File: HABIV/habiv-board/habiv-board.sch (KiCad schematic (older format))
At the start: 129 parts, among them IC1 RTC_PCF8523T, J1 Micro_SD_Card_Det, J10 Conn_01x02_Female, J11 Conn_01x02_Female, J12 Conn_01x02_Female, J13 Conn_01x02_Female, J14 Conn_01x02_Female, J15 Conn_01x02_Female, J16 Conn_01x02_Female, J17 Conn_01x03_Male, J18 Conn_01x03_Male, J19 Conn_01x03_Male, J2 Conn_ARM_JTAG_SWD_20, J20 Conn_01x05_Male, J21 Conn_01x04_Male, J3 Conn_01x02_Male, J4 Conn_01x16_Male, J5 Conn_01x03_Male, J6 Conn_01x16_Male, J7 Conn_01x16_Male, J8 Conn_01x02_Female, J9 Conn_01x02_Male, Q1 32.768KHz, SW1 SW_DPST_x2, U1 STM32F401RET6, U2 MAX31855, U3 FGPMMOPA6H, U4 TPS564208, U5 TPS564208, U6 LSM9DS1TR, U7 MS560702BA03-00, Y1 32.768MHz

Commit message: Turned IMU into breakout pins, minor changes, unfinished!
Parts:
- removed C11, C12, C19: 100n, Capacitor_SMD:C_0805_2012Metric, symbol Device:C_Small
- removed C15: 10u, Capacitor_SMD:C_0805_2012Metric, symbol Device:C_Small
- removed C18: 10n, Capacitor_SMD:C_0805_2012Metric, symbol Device:C_Small
- removed R25, R32, R33, R37: 0, Resistor_SMD:R_0805_2012Metric, symbol Device:R
- removed U6: LSM9DS1TR, digikey-footprints:LGA-24_3x3.5mm_LSM9DS1, symbol dk_Motion-Sensors-IMUs-Inertial-Measurement-Units:LSM9DS1TR
- added J22: Conn_01x09_Male, Connector_PinHeader_2.54mm:PinHeader_1x09_P2.54mm_Vertical, symbol Connector:Conn_01x09_Male
- added JP1: Jumper, Connector_PinHeader_2.54mm:PinHeader_1x02_P2.54mm_Vertical, symbol Device:Jumper
- added R102, R103: 10K, Resistor_SMD:R_0805_2012Metric_Pad1.15x1.40mm_HandSolder, symbol Device:R
- LED1: footprint Adafruit Ultimate GPS:CHIPLED_0805 -> LED_SMD:LED_0805_2012Metric_Pad1.15x1.40mm_HandSolder
- R104: renamed from 10k4; value R8 -> 10K; footprint Resistor_SMD:R_0805_2012Metric -> Resistor_SMD:R_0805_2012Metric_Pad1.15x1.40mm_HandSolder
- R4: renamed from R?; footprint (none) -> Resistor_SMD:R_0805_2012Metric_Pad1.15x1.40mm_HandSolder
- R5: renamed from R?; footprint (none) -> Resistor_SMD:R_0805_2012Metric
- R6: renamed from 10k2; value R6 -> 10K
- R7: renamed from 10k3; value R7 -> 10K
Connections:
- net +3V3: now also C7.1, J22.1 (Pin_1), J22.6 (Pin_6), J22.7 (Pin_7), JP1.1; no longer 10nF1.2, 1uF1.2, 22uH1.1, U1.13 (VDDA/VREF+)
- net GND: now also J22.3 (Pin_3)
- net PB8: now also J22.4 (Pin_4)
- net PB9: now also J22.5 (Pin_5)
- net PC2: now also J22.8 (Pin_8)
- net PC3: now also J22.9 (Pin_9)
- net at U3.P$1 (VCC): now also JP1.2; no longer C7.1
- net at C8.1, C9.1, J9.2 (Pin_2)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: now also R102.2, R103.2; no longer U4.5 (EN), U5.5 (EN)
- new net: 10nF1.2, 1uF1.2, 22uH1.1, U1.13 (VDDA/VREF+)
- new net: R102.1, U4.5 (EN)
- new net: R103.1, U5.5 (EN)
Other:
- note added: "IMU"
- note removed: "C18: 1nF Minimum must be guaranteed under an 11V bias condition\n"
- moved on the sheet: C8, C9, J9

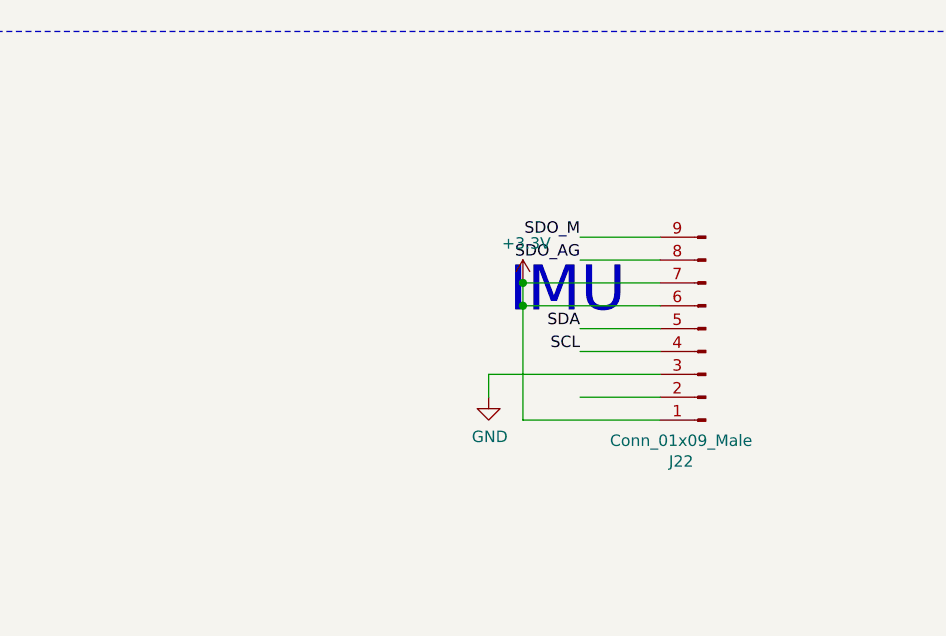
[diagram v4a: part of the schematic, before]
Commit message: Changed IMU pinout, fixed some grounding issues
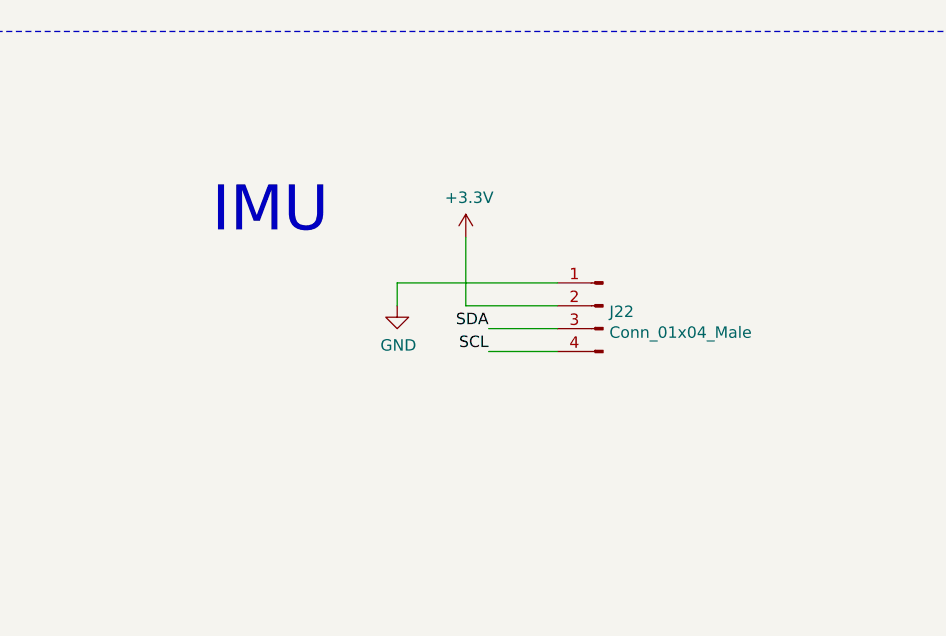
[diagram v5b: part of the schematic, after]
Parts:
- removed J22: Conn_01x09_Male, Connector_PinHeader_2.54mm:PinHeader_1x09_P2.54mm_Vertical, symbol Connector:Conn_01x09_Male
- added J22: Conn_01x04_Male, symbol Connector:Conn_01x04_Male
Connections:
- net +3V3: now also J22.2 (Pin_2)
- net GND: now also J22.1 (Pin_1)
- net PB8: now also J22.4 (Pin_4)
- net PB9: now also J22.3 (Pin_3)
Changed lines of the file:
@@
 	15550 5850 16100 5850
-Wire Wire Line
-	17900 9600 17550 9600
-Wire Wire Line
-	17900 9800 17550 9800
-Wire Wire Line
-	17900 9500 17550 9500
-Wire Wire Line
-	17900 9100 17550 9100
-$Comp
-L power:+3.3V #PWR0110
-U 1 1 5F78A482
-P 17300 9300
-F 0 "#PWR0110" H 17300 9150 50  0001 C CNN
-F 1 "+3.3V" H 17315 9473 50  0000 C CNN
-F 2 "" H 17300 9300 50  0001 C CNN
-F 3 "" H 17300 9300 50  0001 C CNN
-	1    17300 9300
-	1    0    0    -1
-$EndComp
-Text Label 17550 9600 2    50   ~ 0
-SCL
-Text Label 17550 9500 2    50   ~ 0
-SDA
-Text Label 17550 9100 2    50   ~ 0
-SDO_M
-Wire Wire Line
-	17150 9700 17150 9800
-Wire Wire Line
-	17150 9700 17900 9700
-$Comp
-L power:GND #PWR0127
-U 1 1 5F8191BD
-P 17150 9800
-F 0 "#PWR0127" H 17150 9550 50  0001 C CNN
-F 1 "GND" H 17155 9627 50  0000 C CNN
-F 2 "" H 17150 9800 50  0001 C CNN
-F 3 "" H 17150 9800 50  0001 C CNN
-	1    17150 9800
-	1    0    0    -1
-$EndComp
-Wire Wire Line
-	17300 9900 17900 9900
-Wire Wire Line
-	17300 9300 17900 9300
-Text Notes 17750 9450 2    197  ~ 0
-IMU
 Wire Wire Line
 	15550 6650 17050 6650
@@
 Wire Wire Line
 	11450 13850 11450 14350
+Text Notes 16450 9100 2    197  ~ 0
+IMU
+$Comp
+L Connector:Conn_01x04_Male J22
+U 1 1 5E7A5579
+P 17650 9400
+F 0 "J22" H 17622 9374 50  0000 R CNN
+F 1 "Conn_01x04_Male" H 17622 9283 50  0000 R CNN
+F 2 "" H 17650 9400 50  0001 C CNN
+F 3 "~" H 17650 9400 50  0001 C CNN
+	1    17650 9400
+	-1   0    0    -1
+$EndComp
 Wire Wire Line
-	17300 9400 17900 9400
+	17450 9300 16750 9300
+Wire Wire Line
+	16750 9300 16750 9400
+Wire Wire Line
+	17450 9400 17050 9400
+Wire Wire Line
+	17050 9400 17050 9100
+Wire Wire Line
+	17450 9500 17150 9500
+Wire Wire Line
+	17450 9600 17150 9600
+Text Label 17150 9500 2    50   ~ 0
+SDA
+Text Label 17150 9600 2    50   ~ 0
+SCL
 $Comp
-L Connector:Conn_01x09_Male J22
-U 1 1 5F044D94
-P 18100 9500
-F 0 "J22" H 18208 10081 50  0000 C CNN
-F 1 "Conn_01x09_Male" H 18208 9990 50  0000 C CNN
-F 2 "Connector_PinHeader_2.54mm:PinHeader_1x09_P2.54mm_Vertical" H 18208 9989 50  0001 C CNN
-F 3 "~" H 18100 9500 50  0001 C CNN
-	1    18100 9500
-	-1   0    0    1
+L power:GND #PWR?
+U 1 1 5E8E2F4E
+P 16750 9400
+F 0 "#PWR?" H 16750 9150 50  0001 C CNN
+F 1 "GND" H 16755 9227 50  0000 C CNN
+F 2 "" H 16750 9400 50  0001 C CNN
+F 3 "" H 16750 9400 50  0001 C CNN
+	1    16750 9400
+	1    0    0    -1
 $EndComp
-Text Label 17550 9200 2    50   ~ 0
-SDO_AG
-Wire Wire Line
-	17900 9200 17550 9200
-Wire Wire Line
-	17300 9300 17300 9400
-Connection ~ 17300 9300
-Wire Wire Line
-	17300 9400 17300 9900
-Connection ~ 17300 9400
+$Comp
+L power:+3.3V #PWR?
+U 1 1 5E8E44D3
+P 17050 9100
+F 0 "#PWR?" H 17050 8950 50  0001 C CNN
+F 1 "+3.3V" H 17065 9273 50  0000 C CNN
+F 2 "" H 17050 9100 50  0001 C CNN
+F 3 "" H 17050 9100 50  0001 C CNN
+	1    17050 9100
+	1    0    0    -1
+$EndComp
 $EndSCHEMATC
